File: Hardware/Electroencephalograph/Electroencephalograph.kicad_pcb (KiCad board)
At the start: 2 copper layers, 90 x 90 mm, 339 parts, among them J1 Conn_01x08_Male, J2 Conn_01x08_Male, J3 Conn_01x04_Female, J4 Conn_01x04_Female, J5 USB_B_Micro, J6 Conn_01x02_Female, J7 Conn_01x04_Female, J8 Conn_01x02_Male, Q1 FDV304P, Q2 FDV304P, U1 ADS1298IPAG, U10 TPS60403, U11 L78L33_SO8, U12 ESP-12E, U2 OPA330xxD, U3 STM32F030K6Tx, U4 THI3-0511, U5 ADUM2401BRWZ, U6 FT200XD, U7 LP5912-1.8DRVT, U8 LP5912-1.8DRVT, U9 LP5912-1.8DRVT, Y1 20MHz

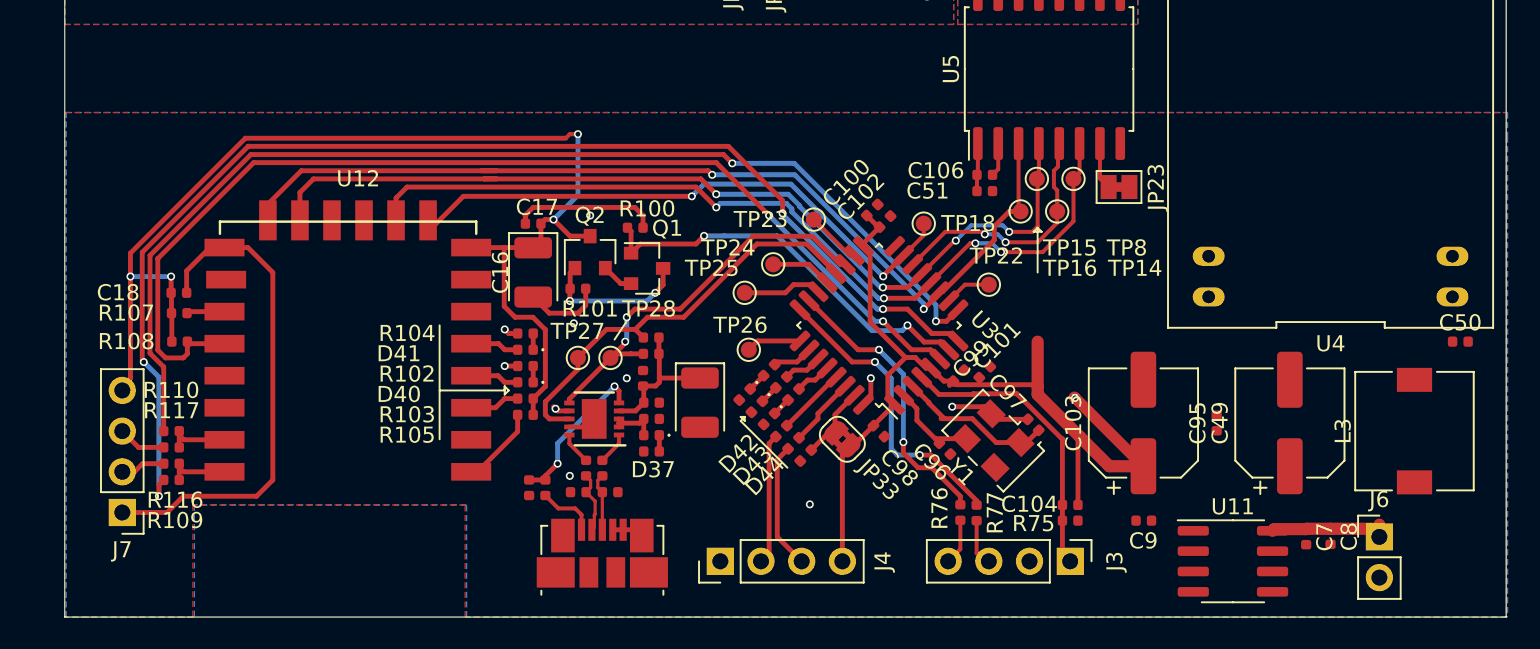
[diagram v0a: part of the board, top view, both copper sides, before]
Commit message: Add draft of poqer supply routing for digital part.
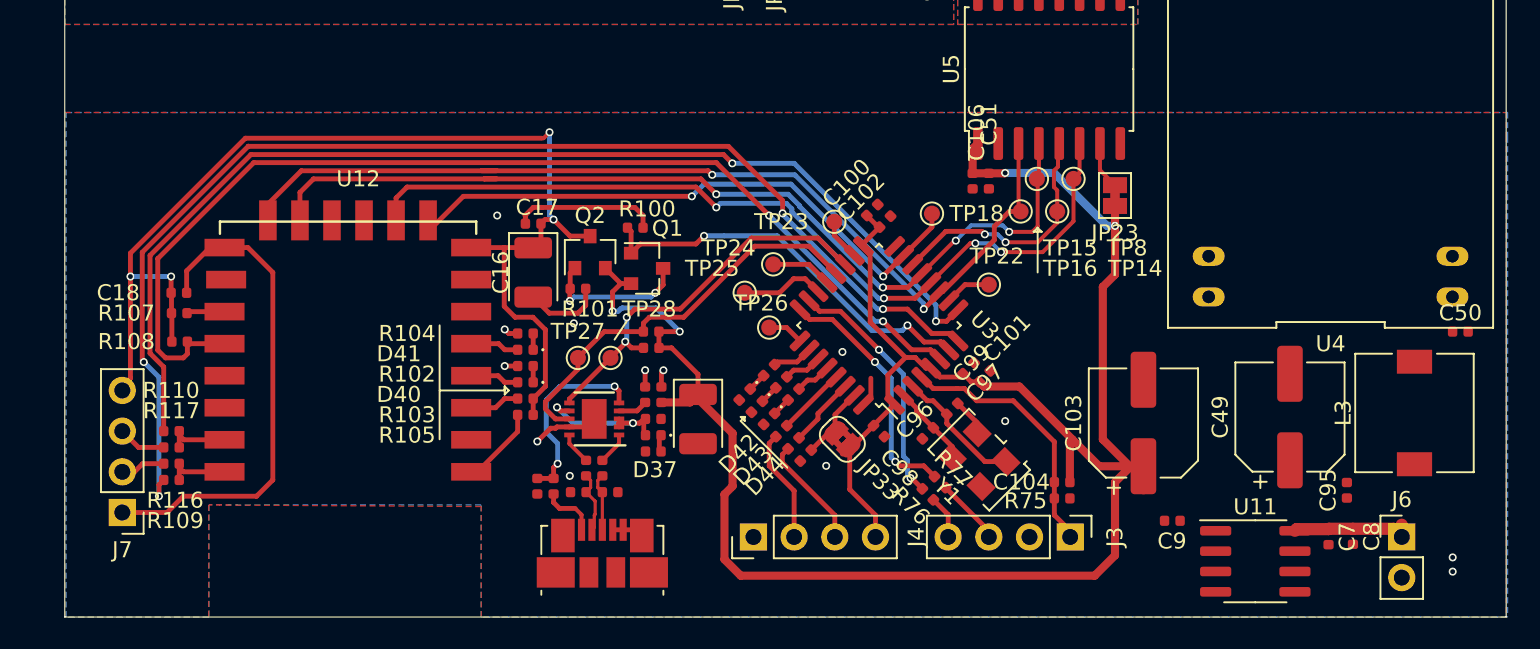
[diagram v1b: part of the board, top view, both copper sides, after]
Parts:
- moved C95 9.15 mm to (130.1, 92.1)
- moved C97 5.15 mm to (105.4, 87.0), turned to 225 degrees
- moved R77 2.98 mm to (104.7, 91.6), turned to 315 degrees
- moved J4 2.57 mm to (93.0, 95.0)
- moved R76 2.32 mm to (103.9, 92.3), turned to 315 degrees
- moved TP26 1.88 mm to (94.0, 81.9)
- moved C9 1.78 mm to (119.2, 94.0)
- moved J3 1.52 mm to (112.8, 95.0)
- moved R75 1.51 mm to (112.3, 91.6)
- moved Y1 1.48 mm to (107.1, 90.2)
- moved C104 1.48 mm to (112.3, 92.6)
- moved C96 1.43 mm to (103.9, 88.5), turned to 45 degrees
- moved C7 1.40 mm to (128.9, 95.0)
- moved C8 1.40 mm to (130.4, 95.0)
- moved J6 1.40 mm to (133.5, 95.0)
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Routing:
- net DP_VDD: track 71.2 -> 139.5 mm, vias 1 -> 4
- net Net-(C109-Pad2): track 4.27 -> 9.18 mm, vias 1 -> 2
- net /DataProcessing/SWCLK: track 18.9 -> 15.7 mm
- net /DataProcessing/SWDIO: track 18.0 -> 15.5 mm
- net Net-(R78-Pad2): track 9.79 -> 12.1 mm
- net Net-(C16-Pad1): track 74.5 -> 72.4 mm
- net /DataProcessing/NRST: track 18.3 -> 16.3 mm
- net Net-(C97-Pad2): track 9.87 -> 8.10 mm
- net Net-(J3-Pad3): track 3.00 -> 4.20 mm
- net Net-(TP26-Pad1): track 3.42 -> 2.27 mm
- net Net-(J4-Pad2): track 8.17 -> 7.08 mm
- net Net-(J4-Pad3): track 7.93 -> 7.01 mm
- net CS_ESP: track 38.3 -> 39.1 mm
- net Net-(TP23-Pad1): track 3.45 -> 2.62 mm
- net SDA: track 26.6 -> 25.8 mm
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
